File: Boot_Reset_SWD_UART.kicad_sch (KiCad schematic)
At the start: 17 parts, among them J6 Conn_ARM_JTAG_SWD_10, J7 DEBUG_UART, J8 Conn_02x05_Odd_Even, Q2 S8050, SW1 SW_RESET

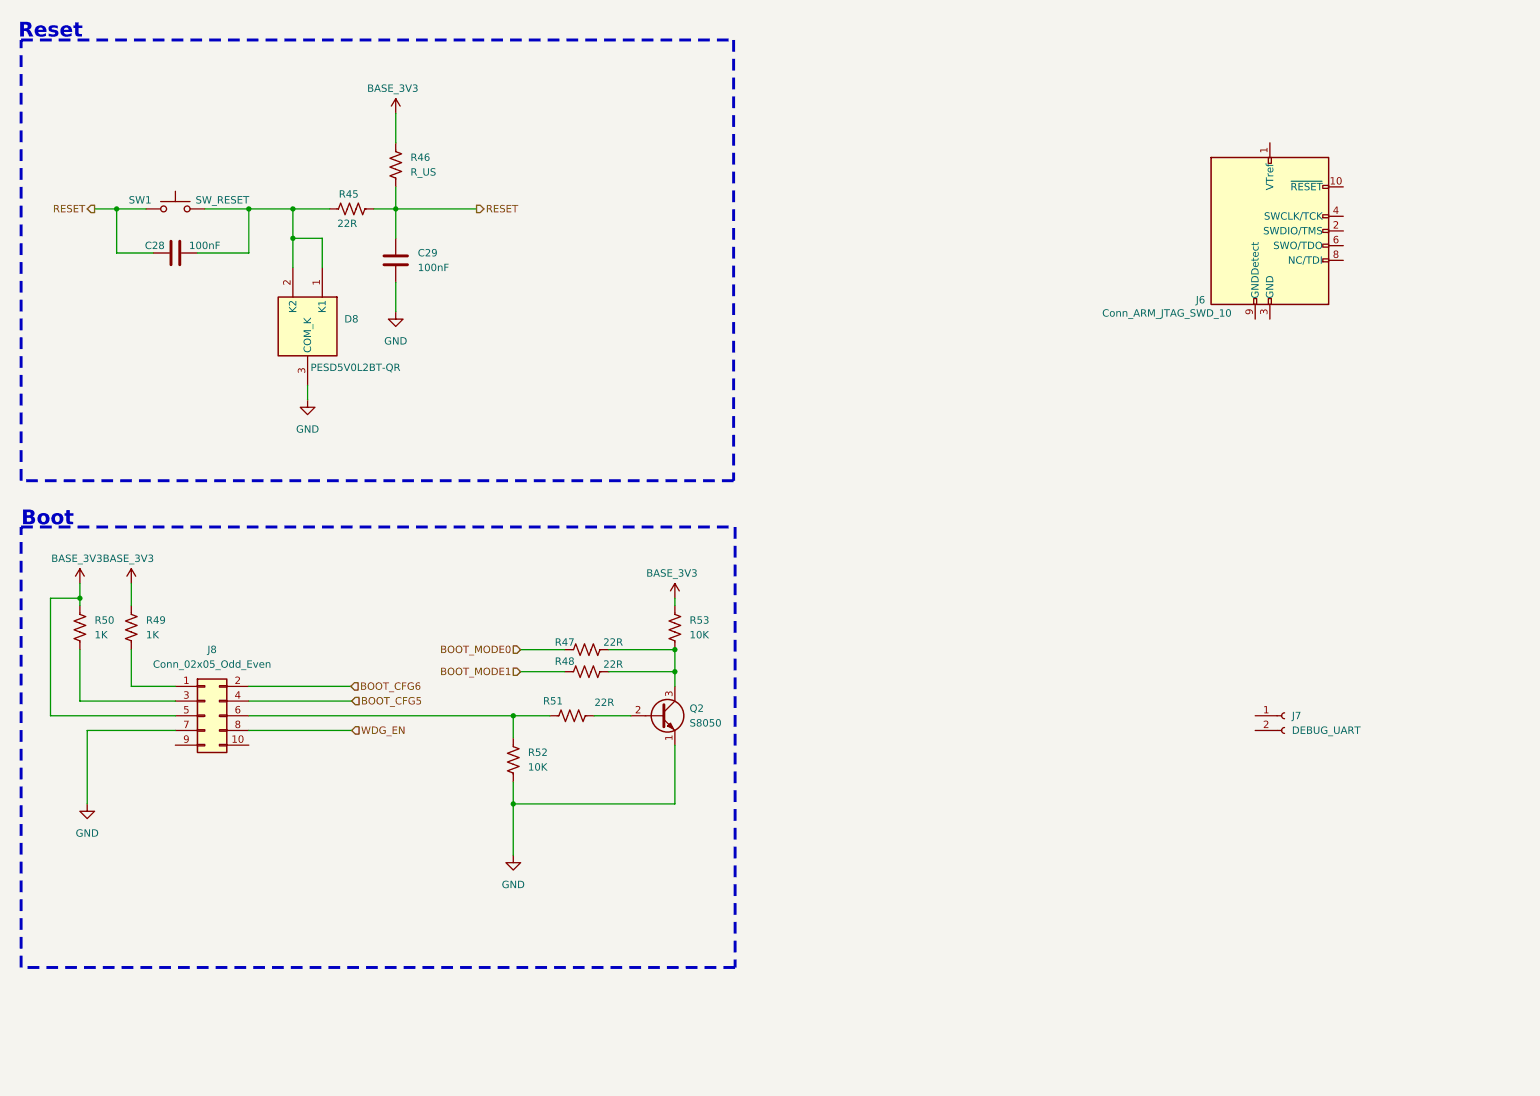
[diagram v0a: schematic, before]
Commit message: 2026 08 16 原理图完成，下一步制作分配未完成的器件封装，准备layout
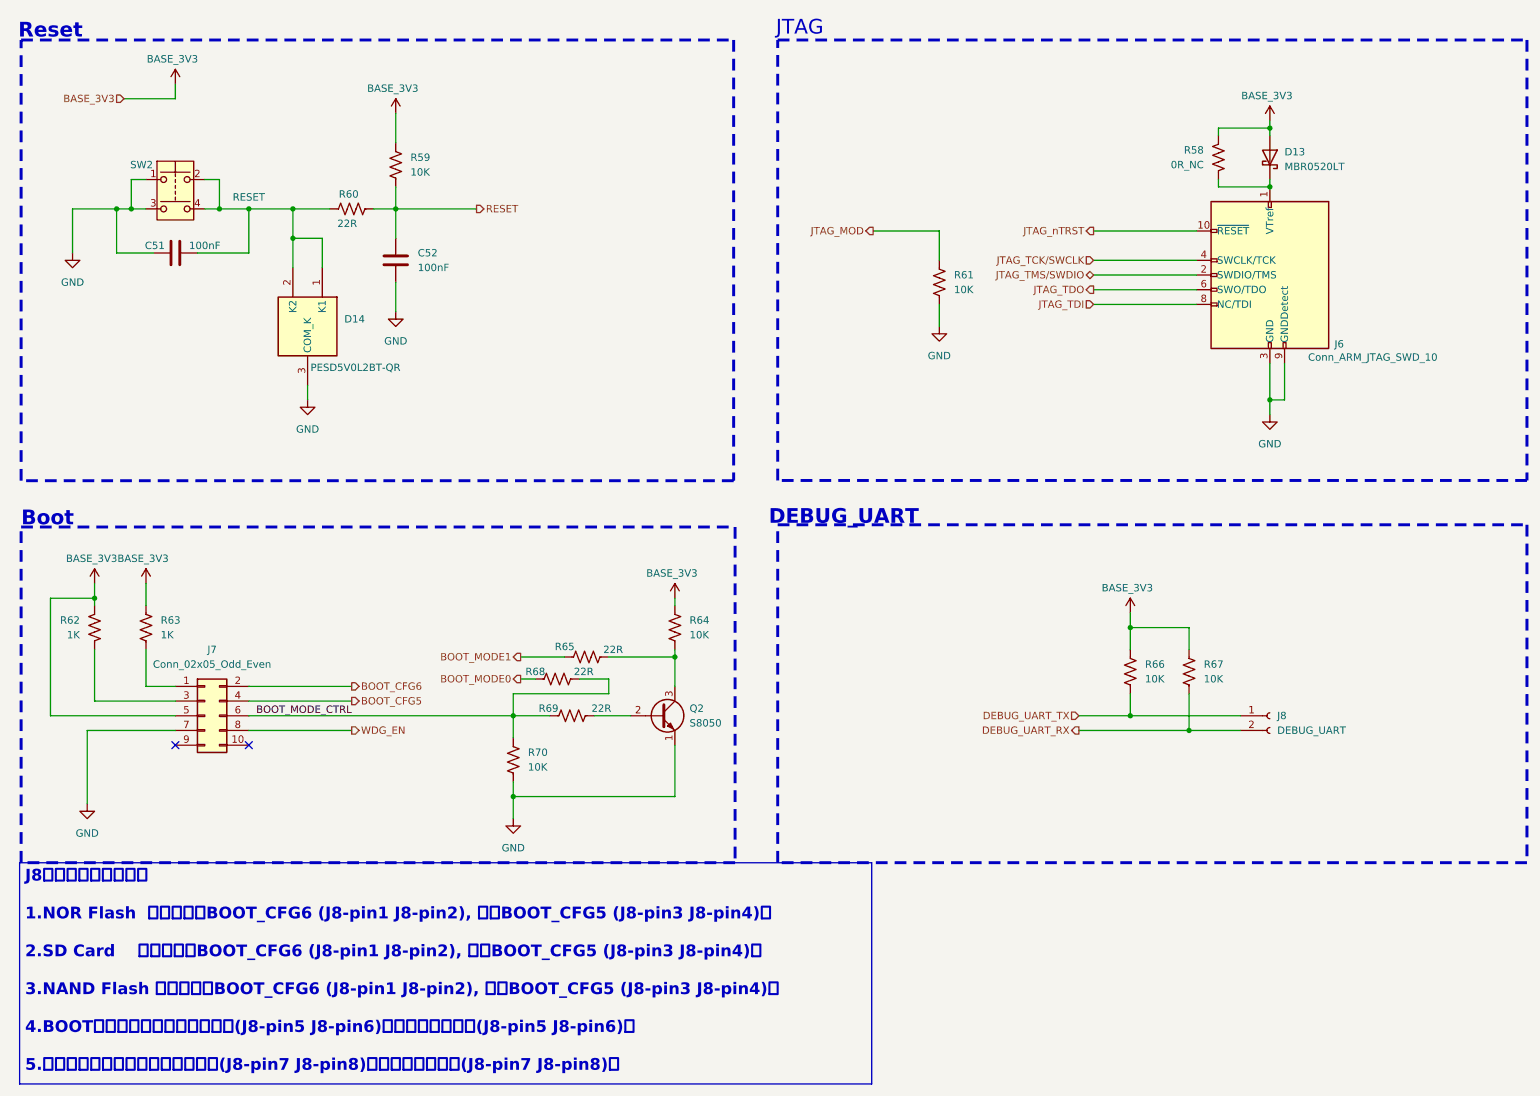
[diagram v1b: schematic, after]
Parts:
- removed R47: 22R, symbol Device:R_US
- removed SW1: SW_RESET, symbol Switch:SW_Push
- added D13: MBR0520LT, Diode_SMD:D_SOD-123, symbol Diode:MBR0520LT
- added R58: 0R_NC, Capacitor_SMD:C_0603_1608Metric_Pad1.08x0.95mm_HandSolder, symbol Device:R_US
- added R61, R66, R67: 10K, Capacitor_SMD:C_0805_2012Metric_Pad1.18x1.45mm_HandSolder, symbol Device:R_US
- added R68: 22R, Capacitor_SMD:C_0603_1608Metric_Pad1.08x0.95mm_HandSolder, symbol Device:R_US
- added SW2: RESET, symbol Switch:SW_Push_Dual
- C51: renamed from C28; footprint (none) -> Capacitor_SMD:C_0603_1608Metric_Pad1.08x0.95mm_HandSolder
- C52: renamed from C29; footprint (none) -> Capacitor_SMD:C_0603_1608Metric_Pad1.08x0.95mm_HandSolder
- D14: renamed from D8; footprint SOT95P230X110-3N -> UPT:SOT95P230X110-3N
- R59: renamed from R46; value R_US -> 10K; footprint (none) -> Capacitor_SMD:C_0805_2012Metric_Pad1.18x1.45mm_HandSolder
- R60: renamed from R45; footprint (none) -> Capacitor_SMD:C_0603_1608Metric_Pad1.08x0.95mm_HandSolder
- R62: renamed from R50; footprint (none) -> Capacitor_SMD:C_0805_2012Metric_Pad1.18x1.45mm_HandSolder
- R63: renamed from R49; footprint (none) -> Capacitor_SMD:C_0805_2012Metric_Pad1.18x1.45mm_HandSolder
- R64: renamed from R53; footprint (none) -> Capacitor_SMD:C_0805_2012Metric_Pad1.18x1.45mm_HandSolder
- R65: renamed from R48; footprint (none) -> Capacitor_SMD:C_0603_1608Metric_Pad1.08x0.95mm_HandSolder
- R69: renamed from R51; footprint (none) -> Capacitor_SMD:C_0603_1608Metric_Pad1.08x0.95mm_HandSolder
- R70: renamed from R52; footprint (none) -> Capacitor_SMD:C_0805_2012Metric_Pad1.18x1.45mm_HandSolder
- renumbered J8 to J7, J7 to J8
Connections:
- net BASE_3V3: now also D13.2 (A), R58.1, R66.1, R67.1
- net BOOT_MODE0: now also R68.1
- net GND: now also C51.1, J6.3 (GND), J6.5 (GND), J6.9 (GNDDetect), R61.2, SW2.1, SW2.3
- net RESET: no longer C51.1
- net BOOT_MODE_CTRL: now reaches J7.6 (Pin_6), R69.2, R70.1
- net BOOT_MODE_CTRL: now also R68.2
- net at C51.2, D14.1 (K1), D14.2 (K2)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: now also SW2.2, SW2.4
- net at J6.1 (VTref): now also D13.1 (K), R58.2
- net JTAG_nTRST: now reaches J6.10 (~{RESET})
- net JTAG_TMS/SWDIO: now reaches J6.2 (SWDIO/TMS)
- net JTAG_TCK/SWCLK: now reaches J6.4 (SWCLK/TCK)
- net JTAG_TDO: now reaches J6.6 (SWO/TDO)
- net JTAG_TDI: now reaches J6.8 (NC/TDI)
- net DEBUG_UART_TX: now reaches J8.1 (Pin_1)
- net DEBUG_UART_TX: now also R66.2
- net DEBUG_UART_RX: now reaches J8.2 (Pin_2)
- net DEBUG_UART_RX: now also R67.2
- new net JTAG_MOD: R61.1
- no-connect marks 0 -> 2
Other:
- note added: "DEBUG_UART"
- note added: "JTAG"
- moved on the sheet: J6, J8, R62, R63, R65

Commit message: 2026 08 24 画图完成，准备生产
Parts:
- removed SW2: RESET, symbol Switch:SW_Push_Dual
- added SW2: SW_Push_Dual, UPT:SW-TH_4P-L6.0-W6.0-P4.50-LS6.5, symbol UPT:SW_Push_Dual
- Q2: footprint Package_TO_SOT_THT:TO-92_Inline -> Package_TO_SOT_SMD:SOT-23_Handsoldering
- R59: footprint Capacitor_SMD:C_0805_2012Metric_Pad1.18x1.45mm_HandSolder -> Capacitor_SMD:C_0603_1608Metric_Pad1.08x0.95mm_HandSolder
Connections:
- net GND: now also SW2.1, SW2.2
- net at C51.2, D14.1 (K1), D14.2 (K2)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: now also SW2.3, SW2.4
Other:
- moved on the sheet: D13, R58
